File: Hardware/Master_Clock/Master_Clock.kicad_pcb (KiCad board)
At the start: 2 copper layers, 20 x 67 mm, 47 parts, among them J1 Phoenix Contact 1935161, J2 Phoenix Contact 1935161, J3 Conn_01x03_Pin, Q1 BC847, SW1 SW_Push, SW2 SW_Push, U1 LT1178S8, U2 LT8330, U3 OP193FS, U4 AP7370-18W5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

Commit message: DRC.
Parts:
- moved J1 0.14 mm to (160.1, 62.9)
- moved J2 0.14 mm to (155.1, 119.9)
- moved C4 0.10 mm to (145.6, 107.3)
- moved C5 0.10 mm to (145.6, 116.5)
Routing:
- net GND: track 238.6 -> 232.9 mm
- net /MinPulse: track 49.4 -> 46.7 mm
- net +24V: track 29.2 -> 26.7 mm
- net +1V8: track 113.5 -> 111.3 mm
- net Net-(C5-Pad1): track 3.59 -> 1.79 mm
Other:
- board text added: "Master Clock"

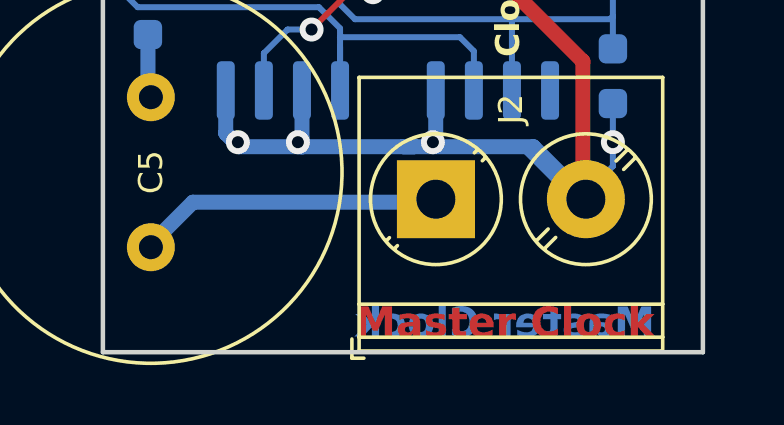
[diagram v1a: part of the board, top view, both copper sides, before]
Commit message: Add some testpoints. Just in case...
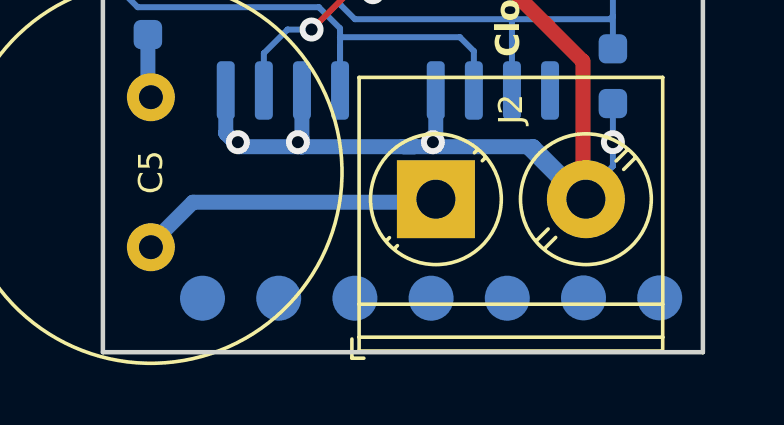
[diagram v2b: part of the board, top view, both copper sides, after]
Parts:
- added REF**: TestPoint_Pad_D1.5mm, TestPoint:TestPoint_Pad_D1.5mm, B.Cu at (152.4, 123.2)
- added REF**: TestPoint_Pad_D1.5mm, TestPoint:TestPoint_Pad_D1.5mm, B.Cu at (157.5, 123.2)
- added REF**: TestPoint_Pad_D1.5mm, TestPoint:TestPoint_Pad_D1.5mm, B.Cu at (154.9, 123.2)
- added REF**: TestPoint_Pad_D1.5mm, TestPoint:TestPoint_Pad_D1.5mm, B.Cu at (149.9, 123.2)
- added REF**: TestPoint_Pad_D1.5mm, TestPoint:TestPoint_Pad_D1.5mm, B.Cu at (160.0, 123.2)
- added REF**: TestPoint_Pad_D1.5mm, TestPoint:TestPoint_Pad_D1.5mm, B.Cu at (162.6, 123.2)
- added REF**: TestPoint_Pad_D1.5mm, TestPoint:TestPoint_Pad_D1.5mm, B.Cu at (147.3, 123.2)
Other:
- board text removed: "Master Clock"
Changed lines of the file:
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@@
     )
+  )
+  (footprint "TestPoint:TestPoint_Pad_D1.5mm" (layer "B.Cu")
+    (at 152.4 123.2 180)
+    (descr "SMD pad as test Point, diameter 1.5mm")
+    (tags "test point SMD pad")
+    (attr board_only exclude_from_pos_files exclude_from_bom)
+    (fp_text reference "REF**" (at 0 1.648) (layer "B.SilkS") hide
+        (effects (font (size 1 1) (thickness 0.15)) (justify mirror))
+    )
+    (fp_text value "TestPoint_Pad_D1.5mm" (at 0 -1.75) (layer "B.Fab") hide
+        (effects (font (size 1 1) (thickness 0.15)) (justify mirror))
+    )
+    (fp_text user "${REFERENCE}" (at 0 1.65) (layer "B.Fab") hide
+        (effects (font (size 1 1) (thickness 0.15)) (justify mirror))
+    )
+    (fp_circle (center 0 0) (end 0 -0.95)
+      (stroke (width 0.12) (type solid)) (fill none) (layer "B.SilkS"))
+    (fp_circle (center 0 0) (end 1.25 0)
+      (stroke (width 0.05) (type solid)) (fill none) (layer "B.CrtYd"))
+    (pad "1" smd circle (at 0 0 180) (size 1.5 1.5) (layers "B.Cu" "B.Mask"))
   )
   (footprint "Capacitor_SMD:C_0603_1608Metric_Pad1.08x0.95mm_HandSolder" locked (layer "B.Cu")
@@
     )
   )
+  (footprint "TestPoint:TestPoint_Pad_D1.5mm" (layer "B.Cu")
+    (at 157.48 123.2 180)
+    (descr "SMD pad as test Point, diameter 1.5mm")
+    (tags "test point SMD pad")
+    (attr board_only exclude_from_pos_files exclude_from_bom)
+    (fp_text reference "REF**" (at 0 1.648) (layer "B.SilkS") hide
+        (effects (font (size 1 1) (thickness 0.15)) (justify mirror))
+    )
+    (fp_text value "TestPoint_Pad_D1.5mm" (at 0 -1.75) (layer "B.Fab") hide
+        (effects (font (size 1 1) (thickness 0.15)) (justify mirror))
+    )
+    (fp_text user "${REFERENCE}" (at 0 1.65) (layer "B.Fab") hide
+        (effects (font (size 1 1) (thickness 0.15)) (justify mirror))
+    )
+    (fp_circle (center 0 0) (end 0 -0.95)
+      (stroke (width 0.12) (type solid)) (fill none) (layer "B.SilkS"))
+    (fp_circle (center 0 0) (end 1.25 0)
+      (stroke (width 0.05) (type solid)) (fill none) (layer "B.CrtYd"))
+    (pad "1" smd circle (at 0 0 180) (size 1.5 1.5) (layers "B.Cu" "B.Mask"))
+  )
   (footprint "Inductor_SMD:L_1812_4532Metric_Pad1.30x3.40mm_HandSolder" locked (layer "B.Cu")
     (at 160.5 99.5 -90)
@@
     )
   )
+  (footprint "TestPoint:TestPoint_Pad_D1.5mm" (layer "B.Cu")
+    (at 154.94 123.2 180)
+    (descr "SMD pad as test Point, diameter 1.5mm")
+    (tags "test point SMD pad")
+    (attr board_only exclude_from_pos_files exclude_from_bom)
+    (fp_text reference "REF**" (at 0 1.648) (layer "B.SilkS") hide
+        (effects (font (size 1 1) (thickness 0.15)) (justify mirror))
+    )
+    (fp_text value "TestPoint_Pad_D1.5mm" (at 0 -1.75) (layer "B.Fab") hide
+        (effects (font (size 1 1) (thickness 0.15)) (justify mirror))
+    )
+    (fp_text user "${REFERENCE}" (at 0 1.65) (layer "B.Fab") hide
+        (effects (font (size 1 1) (thickness 0.15)) (justify mirror))
+    )
+    (fp_circle (center 0 0) (end 0 -0.95)
+      (stroke (width 0.12) (type solid)) (fill none) (layer "B.SilkS"))
+    (fp_circle (center 0 0) (end 1.25 0)
+      (stroke (width 0.05) (type solid)) (fill none) (layer "B.CrtYd"))
+    (pad "1" smd circle (at 0 0 180) (size 1.5 1.5) (layers "B.Cu" "B.Mask"))
+  )
+  (footprint "TestPoint:TestPoint_Pad_D1.5mm" (layer "B.Cu")
+    (at 149.86 123.2 180)
+    (descr "SMD pad as test Point, diameter 1.5mm")
+    (tags "test point SMD pad")
+    (attr board_only exclude_from_pos_files exclude_from_bom)
+    (fp_text reference "REF**" (at 0 1.648) (layer "B.SilkS") hide
+        (effects (font (size 1 1) (thickness 0.15)) (justify mirror))
+    )
+    (fp_text value "TestPoint_Pad_D1.5mm" (at 0 -1.75) (layer "B.Fab") hide
+        (effects (font (size 1 1) (thickness 0.15)) (justify mirror))
+    )
+    (fp_text user "${REFERENCE}" (at 0 1.65) (layer "B.Fab") hide
+        (effects (font (size 1 1) (thickness 0.15)) (justify mirror))
+    )
+    (fp_circle (center 0 0) (end 0 -0.95)
+      (stroke (width 0.12) (type solid)) (fill none) (layer "B.SilkS"))
+    (fp_circle (center 0 0) (end 1.25 0)
+      (stroke (width 0.05) (type solid)) (fill none) (layer "B.CrtYd"))
+    (pad "1" smd circle (at 0 0 180) (size 1.5 1.5) (layers "B.Cu" "B.Mask"))
+  )
   (footprint "Resistor_SMD:R_0603_1608Metric_Pad0.98x0.95mm_HandSolder" (layer "B.Cu")
     (at 149 97.5 90)
@@
     )
   )
+  (footprint "TestPoint:TestPoint_Pad_D1.5mm" (layer "B.Cu")
+    (at 160.02 123.19 180)
+    (descr "SMD pad as test Point, diameter 1.5mm")
+    (tags "test point SMD pad")
+    (attr board_only exclude_from_pos_files exclude_from_bom)
+    (fp_text reference "REF**" (at 0 1.648) (layer "B.SilkS") hide
+        (effects (font (size 1 1) (thickness 0.15)) (justify mirror))
+    )
+    (fp_text value "TestPoint_Pad_D1.5mm" (at 0 -1.75) (layer "B.Fab") hide
+        (effects (font (size 1 1) (thickness 0.15)) (justify mirror))
+    )
+    (fp_text user "${REFERENCE}" (at 0 1.65) (layer "B.Fab") hide
+        (effects (font (size 1 1) (thickness 0.15)) (justify mirror))
+    )
+    (fp_circle (center 0 0) (end 0 -0.95)
+      (stroke (width 0.12) (type solid)) (fill none) (layer "B.SilkS"))
+    (fp_circle (center 0 0) (end 1.25 0)
+      (stroke (width 0.05) (type solid)) (fill none) (layer "B.CrtYd"))
+    (pad "1" smd circle (at 0 0 180) (size 1.5 1.5) (layers "B.Cu" "B.Mask"))
+  )
+  (footprint "TestPoint:TestPoint_Pad_D1.5mm" (layer "B.Cu")
+    (at 162.56 123.19 180)
+    (descr "SMD pad as test Point, diameter 1.5mm")
+    (tags "test point SMD pad")
+    (attr board_only exclude_from_pos_files exclude_from_bom)
+    (fp_text reference "REF**" (at 0 1.648) (layer "B.SilkS") hide
+        (effects (font (size 1 1) (thickness 0.15)) (justify mirror))
+    )
+    (fp_text value "TestPoint_Pad_D1.5mm" (at 0 -1.75) (layer "B.Fab") hide
+        (effects (font (size 1 1) (thickness 0.15)) (justify mirror))
+    )
+    (fp_text user "${REFERENCE}" (at 0 1.65) (layer "B.Fab") hide
+        (effects (font (size 1 1) (thickness 0.15)) (justify mirror))
+    )
+    (fp_circle (center 0 0) (end 0 -0.95)
+      (stroke (width 0.12) (type solid)) (fill none) (layer "B.SilkS"))
+    (fp_circle (center 0 0) (end 1.25 0)
+      (stroke (width 0.05) (type solid)) (fill none) (layer "B.CrtYd"))
+    (pad "1" smd circle (at 0 0 180) (size 1.5 1.5) (layers "B.Cu" "B.Mask"))
+  )
   (footprint "Capacitor_SMD:C_0805_2012Metric_Pad1.18x1.45mm_HandSolder" locked (layer "B.Cu")
     (at 153.5 104.5 180)
@@
     )
   )
+  (footprint "TestPoint:TestPoint_Pad_D1.5mm" (layer "B.Cu")
+    (at 147.32 123.2 180)
+    (descr "SMD pad as test Point, diameter 1.5mm")
+    (tags "test point SMD pad")
+    (attr board_only exclude_from_pos_files exclude_from_bom)
+    (fp_text reference "REF**" (at 0 1.648) (layer "B.SilkS") hide
+        (effects (font (size 1 1) (thickness 0.15)) (justify mirror))
+    )
+    (fp_text value "TestPoint_Pad_D1.5mm" (at 0 -1.75) (layer "B.Fab") hide
+        (effects (font (size 1 1) (thickness 0.15)) (justify mirror))
+    )
+    (fp_text user "${REFERENCE}" (at 0 1.65) (layer "B.Fab") hide
+        (effects (font (size 1 1) (thickness 0.15)) (justify mirror))
+    )
+    (fp_circle (center 0 0) (end 0 -0.95)
+      (stroke (width 0.12) (type solid)) (fill none) (layer "B.SilkS"))
+    (fp_circle (center 0 0) (end 1.25 0)
+      (stroke (width 0.05) (type solid)) (fill none) (layer "B.CrtYd"))
+    (pad "1" smd circle (at 0 0 180) (size 1.5 1.5) (layers "B.Cu" "B.Mask"))
+  )
   (footprint "Resistor_SMD:R_0603_1608Metric_Pad0.98x0.95mm_HandSolder" locked (layer "B.Cu")
     (at 145.5 113.5 -90)
@@
   (gr_rect (start 144 58) (end 164 125)
     (stroke (width 0.15) (type default)) (fill none) (layer "Edge.Cuts"))
-  (gr_text "Master Clock" (at 152.4 124.6) (layer "F.Cu")
-    (effects (font (size 1 1) (thickness 0.2) bold) (justify left bottom))
-  )
   (gr_text "Master Clock\nV1.0 12/2023\nC. Mauderer" (at 157.4 59.8) (layer "B.Cu")
     (effects (font (size 0.6 0.6) (thickness 0.15) bold) (justify left mirror))
   )
-  (gr_text "Master Clock" (at 162.4 124.6) (layer "B.Cu")
-    (effects (font (size 1 1) (thickness 0.2) bold) (justify left bottom mirror))
-  )
   (gr_text "c-mauderer.de/s/master-clock" (at 163 103 90) (layer "F.SilkS")

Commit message: Hardware 1.1
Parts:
- added R15: 2M2, Resistor_SMD:R_0603_1608Metric_Pad0.98x0.95mm_HandSolder, B.Cu at (146.5, 109.2)
- added R16: 2M2, Resistor_SMD:R_0603_1608Metric_Pad0.98x0.95mm_HandSolder, B.Cu at (146.5, 112.8)
- added R17: 2M2, Resistor_SMD:R_0603_1608Metric_Pad0.98x0.95mm_HandSolder, B.Cu at (146.5, 111.0)
- C5: value 470u 50V -> Panasonic FC 180u 63V
- R1, R3: value 10M 1% -> 2M2
- R2: value 10M 1% -> 4M7
- R4: value 750k 1% -> 330k
- moved TP2 7.79 mm to (145.2, 89.2)
- moved R11 1.41 mm to (146.5, 114.5), turned to 180 degrees
- moved U1 1.09 mm to (151.1, 113.8)
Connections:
- U1 pad 1: /MinPulse -> Net-(U1A-+)
- U3 pad 3: /MinPulse -> Net-(U1A-+)
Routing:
- net Net-(U1A-+): track 0.00 -> 23.1 mm
- net /MinPulse: track 46.7 -> 25.9 mm
- net GND: track 232.9 -> 240.5 mm, vias 23 -> 24
- net +1V8: track 111.3 -> 114.7 mm, vias 4 -> 5
- net Net-(U1A--): track 15.9 -> 14.5 mm
- net Net-(R11-Pad1): track 15.7 -> 14.4 mm
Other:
- board text added: "+"
- board text added: "- 3..10V +"
- board text added: "Master Clock V1.1 02/2024 C. Mauderer"
- board text removed: "3..10V"
- board text removed: "Master Clock V1.0 12/2023 C. Mauderer"
